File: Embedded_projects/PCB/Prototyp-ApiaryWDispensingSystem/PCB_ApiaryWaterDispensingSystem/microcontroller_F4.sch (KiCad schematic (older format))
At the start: 76 parts, among them J10 Conn_02x19_Odd_Even, J7 Conn_02x19_Odd_Even, U1 STM32F411RETx, Y2 Crystal_GND23_Small, Y3 Crystal

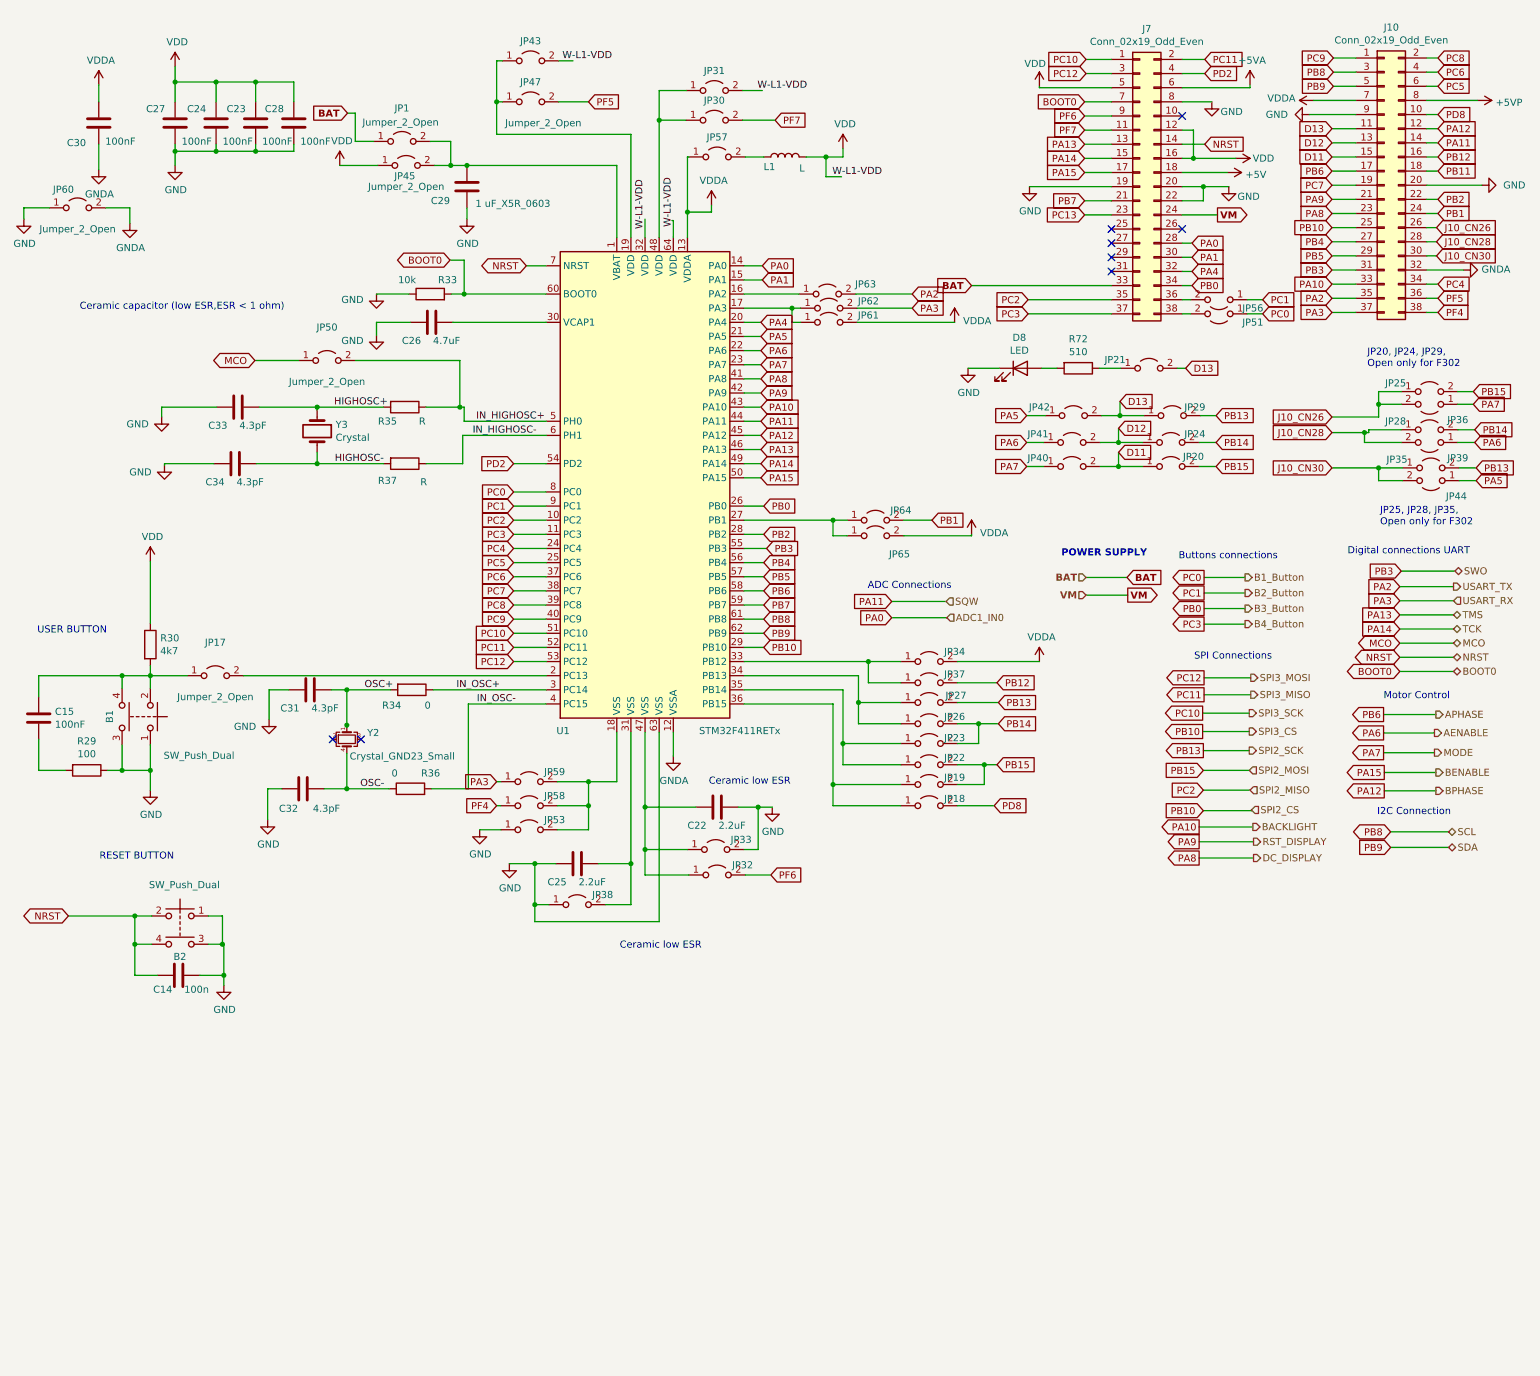
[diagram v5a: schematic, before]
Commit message: update html in readme.RST and improved PCb #3
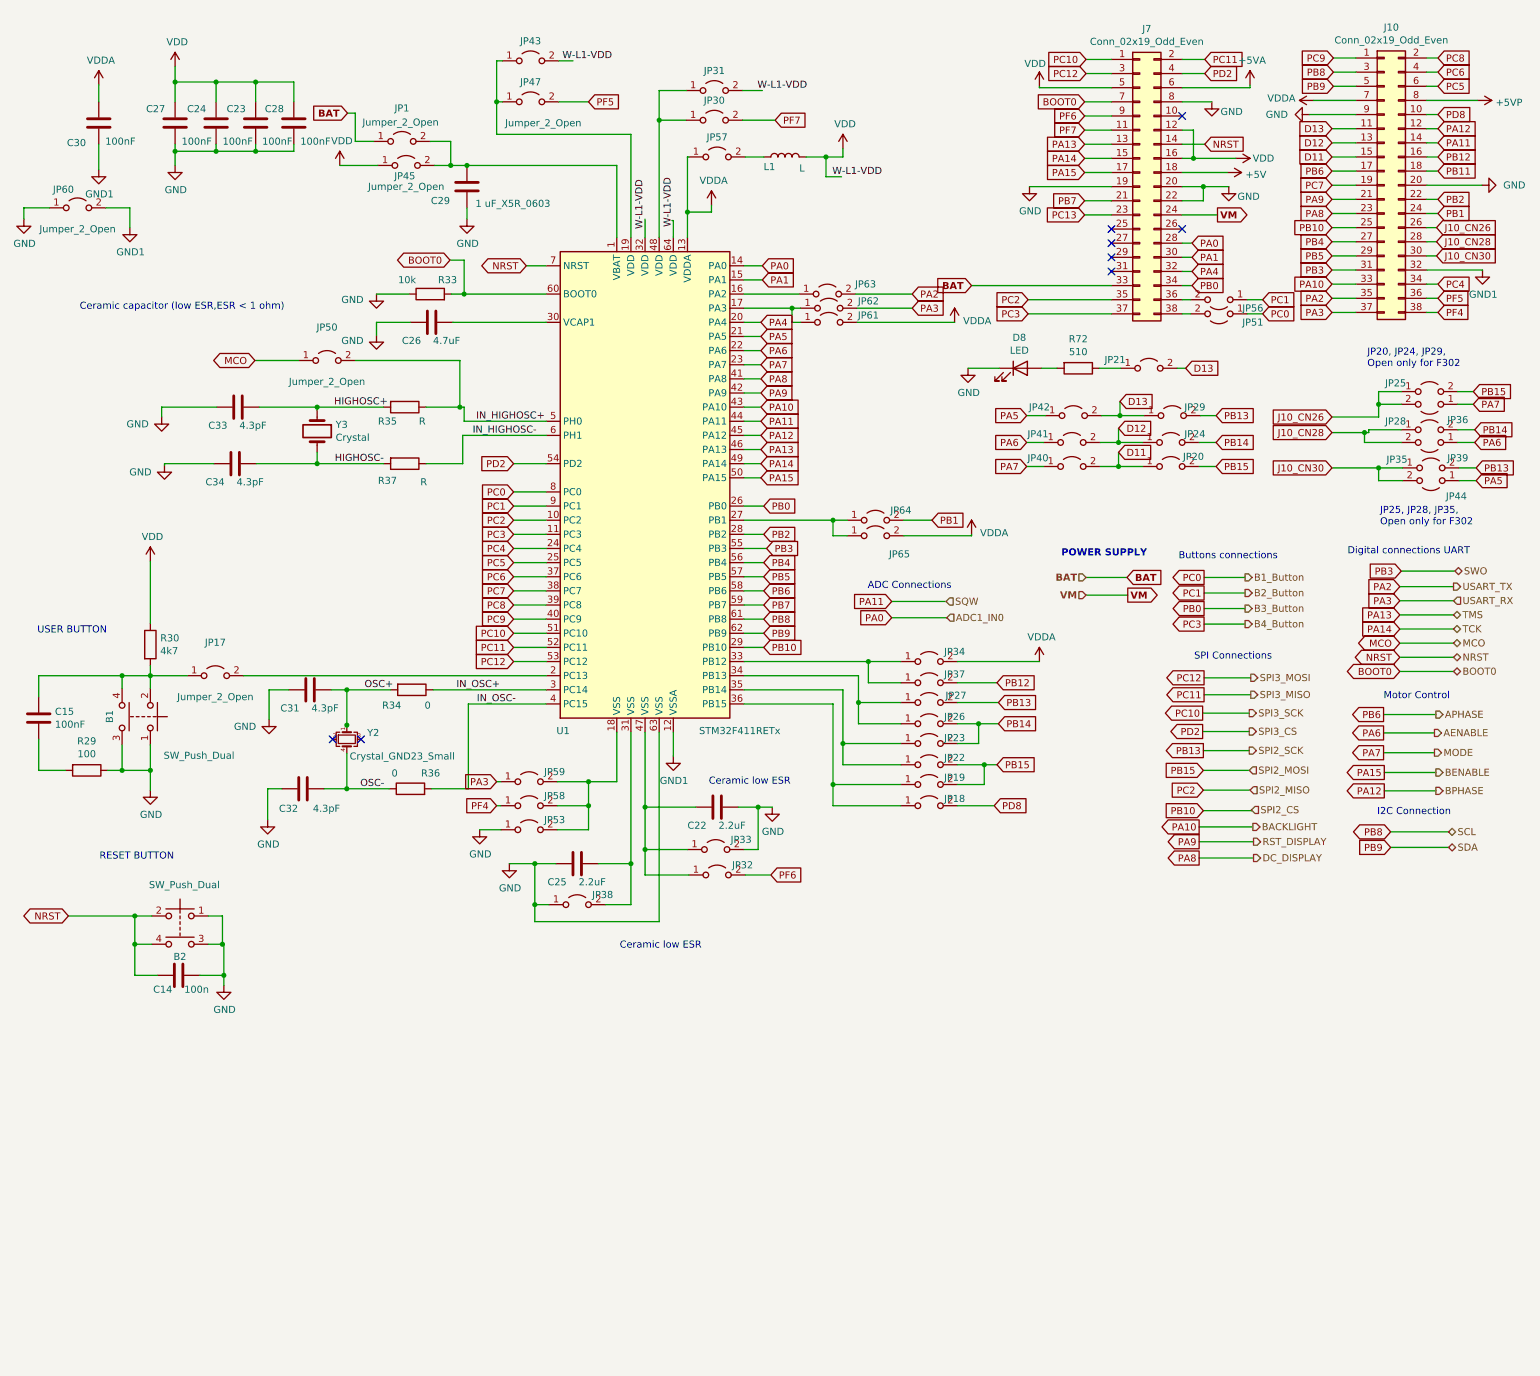
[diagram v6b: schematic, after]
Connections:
- net GNDA renamed GND1
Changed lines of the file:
@@
 	-1   0    0    1
-$EndComp
-$Comp
-L power:GNDA #PWR0108
-U 1 1 67EB896C
-P 1145 1580
-F 0 "#PWR0108" H 1145 1330 50  0001 C CNN
-F 1 "GNDA" H 1150 1407 50  0000 C CNN
-F 2 "" H 1145 1580 50  0001 C CNN
-F 3 "" H 1145 1580 50  0001 C CNN
-	1    1145 1580
-	1    0    0    -1
 $EndComp
 Wire Wire Line
@@
 F 3 "" H 615 1930 50  0001 C CNN
 	1    615  1930
-	1    0    0    -1
-$EndComp
-$Comp
-L power:GNDA #PWR0110
-U 1 1 67EBF91F
-P 1365 1960
-F 0 "#PWR0110" H 1365 1710 50  0001 C CNN
-F 1 "GNDA" H 1370 1787 50  0000 C CNN
-F 2 "" H 1365 1960 50  0001 C CNN
-F 3 "" H 1365 1960 50  0001 C CNN
-	1    1365 1960
 	1    0    0    -1
 $EndComp
@@
 Text Notes 6040 5940 2    50   ~ 0
 Ceramic low ESR
-$Comp
-L power:GNDA #PWR0121
-U 1 1 6814EFF6
-P 5210 5730
-F 0 "#PWR0121" H 5210 5480 50  0001 C CNN
-F 1 "GNDA" H 5215 5557 50  0000 C CNN
-F 2 "" H 5210 5730 50  0001 C CNN
-F 3 "" H 5210 5730 50  0001 C CNN
-	1    5210 5730
-	1    0    0    -1
-$EndComp
 Wire Wire Line
 	5210 5560 5210 5730
@@
 Wire Wire Line
 	1195 1850 1365 1850
-Wire Wire Line
-	1365 1850 1365 1960
 NoConn ~ 3000 5610
 NoConn ~ 2800 5610
@@
 Text GLabel 8955 5425 0    50   Output ~ 0
 PC10
-Text GLabel 8955 5555 0    50   Output ~ 0
-PB10
 Text Notes 10235 5335 0    50   ~ 0
 Motor Control
@@
 Wire Wire Line
 	10620 790  10540 790
-$Comp
-L power:GNDA #PWR0228
-U 1 1 68EF1599
-P 10800 2290
-F 0 "#PWR0228" H 10800 2040 50  0001 C CNN
-F 1 "GNDA" V 10805 2162 50  0000 R CNN
-F 2 "" H 10800 2290 50  0001 C CNN
-F 3 "" H 10800 2290 50  0001 C CNN
-	1    10800 2290
-	0    -1   -1   0
-$EndComp
-Wire Wire Line
-	10800 2290 10540 2290
 Text GLabel 10620 2390 2    50   Input ~ 0
 PC4
@@
 	1    0    0    -1
 $EndComp
+$Comp
+L power:GND1 #PWR0108
+U 1 1 690DACEC
+P 1365 1990
+F 0 "#PWR0108" H 1365 1740 50  0001 C CNN
+F 1 "GND1" H 1370 1817 50  0000 C CNN
+F 2 "" H 1365 1990 50  0001 C CNN
+F 3 "" H 1365 1990 50  0001 C CNN
+	1    1365 1990
+	1    0    0    -1
+$EndComp
+Wire Wire Line
+	1365 1850 1365 1990
+$Comp
+L power:GND1 #PWR0110
+U 1 1 6910BCB4
+P 10935 2290
+F 0 "#PWR0110" H 10935 2040 50  0001 C CNN
+F 1 "GND1" H 10940 2117 50  0000 C CNN
+F 2 "" H 10935 2290 50  0001 C CNN
+F 3 "" H 10935 2290 50  0001 C CNN
+	1    10935 2290
+	1    0    0    -1
+$EndComp
+$Comp
+L power:GND1 #PWR0127
+U 1 1 6910BF54
+P 1145 1580
+F 0 "#PWR0127" H 1145 1330 50  0001 C CNN
+F 1 "GND1" H 1150 1407 50  0000 C CNN
+F 2 "" H 1145 1580 50  0001 C CNN
+F 3 "" H 1145 1580 50  0001 C CNN
+	1    1145 1580
+	1    0    0    -1
+$EndComp
+Wire Wire Line
+	10540 2290 10935 2290
+Text GLabel 8955 5555 0    50   Output ~ 0
+PD2
+$Comp
+L power:GND1 #PWR?
+U 1 1 69218867
+P 5210 5730
+F 0 "#PWR?" H 5210 5480 50  0001 C CNN
+F 1 "GND1" H 5215 5557 50  0000 C CNN
+F 2 "" H 5210 5730 50  0001 C CNN
+F 3 "" H 5210 5730 50  0001 C CNN
+	1    5210 5730
+	1    0    0    -1
+$EndComp
